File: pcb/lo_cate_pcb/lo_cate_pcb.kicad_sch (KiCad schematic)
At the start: 49 parts, among them J1 Conn_01x07_Pin, J2 690-005-299-043, J3 U.FL-R-SMT-110, SW1 MICRO_RESET, SW2 MICRO_ON, SW3 BUTTON1, SW4 BUTTON2, SW5 BUTTON3, U1 STM32F401RETx, U2 BMI323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

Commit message: Final PCB design done
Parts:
- removed J3: U.FL-R-SMT-110, footprints:CONN1_UFL-R_HIR, symbol 2024-06-24_09-28-13:U.FL-R-SMT-110
- added U8: 734120114, footprints:73412-0114_MOL, symbol 2024-06-27_09-08-45:734120114
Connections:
- net GND: now also U8.2 (GROUND), U8.3 (GROUND), U8.4 (GROUND)
- net at U6.9 (ANT): now also U8.1 (SIGNAL)

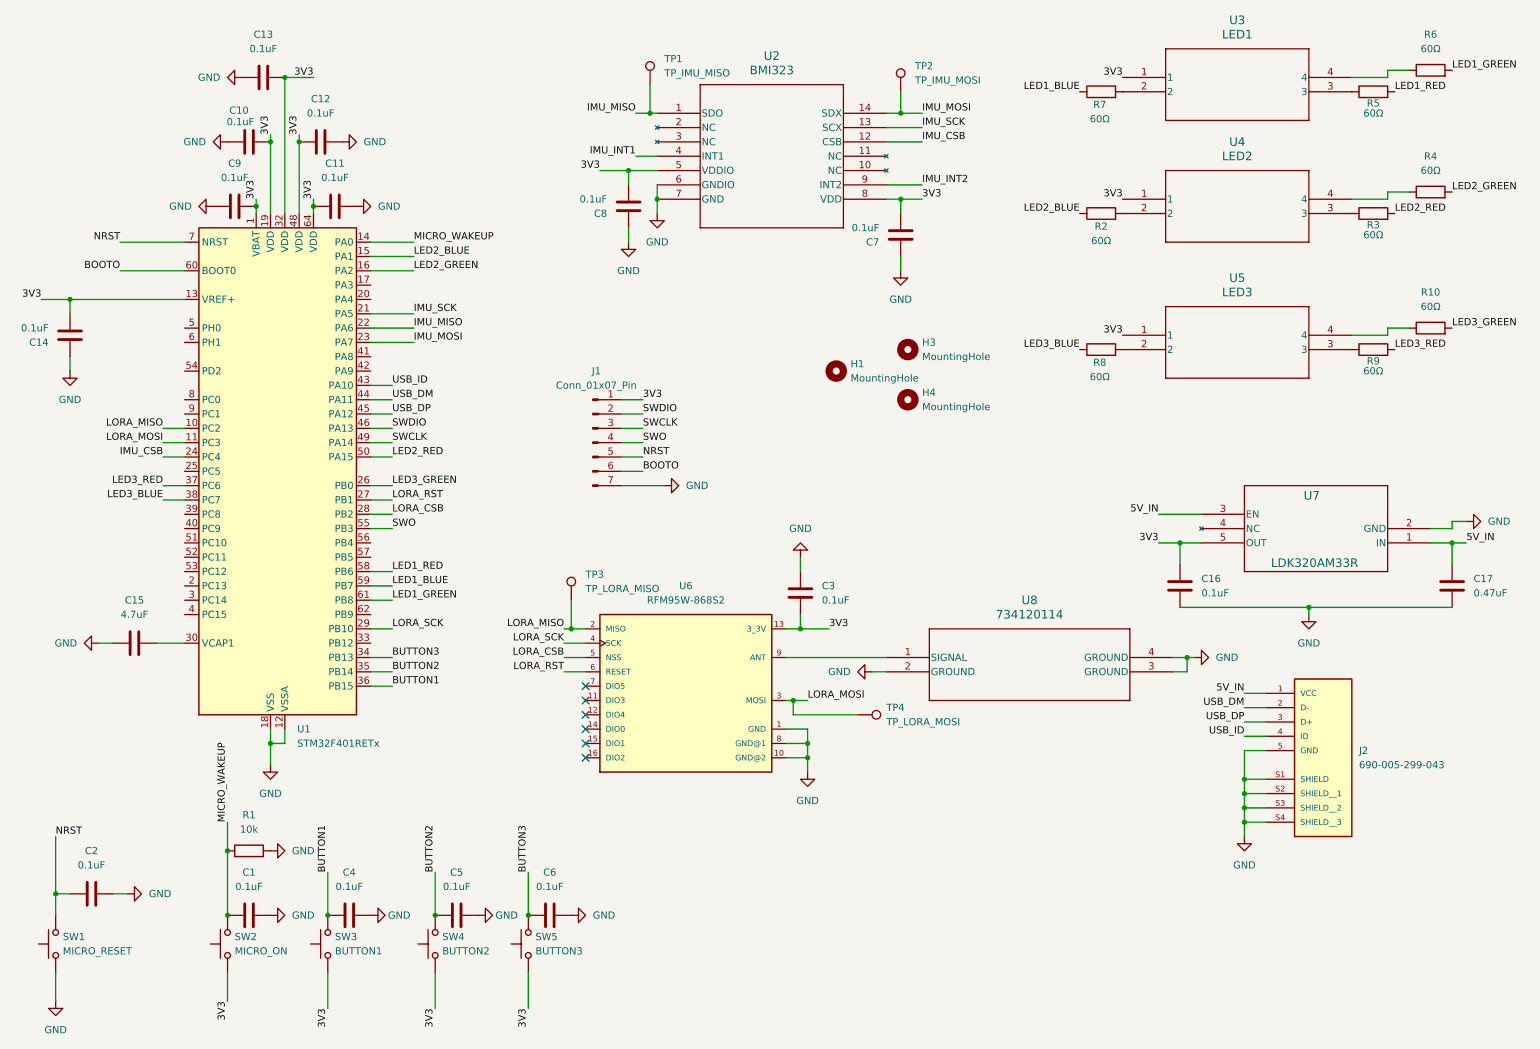
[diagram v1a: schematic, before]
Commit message: Changed PCB to a 4 Layer Version
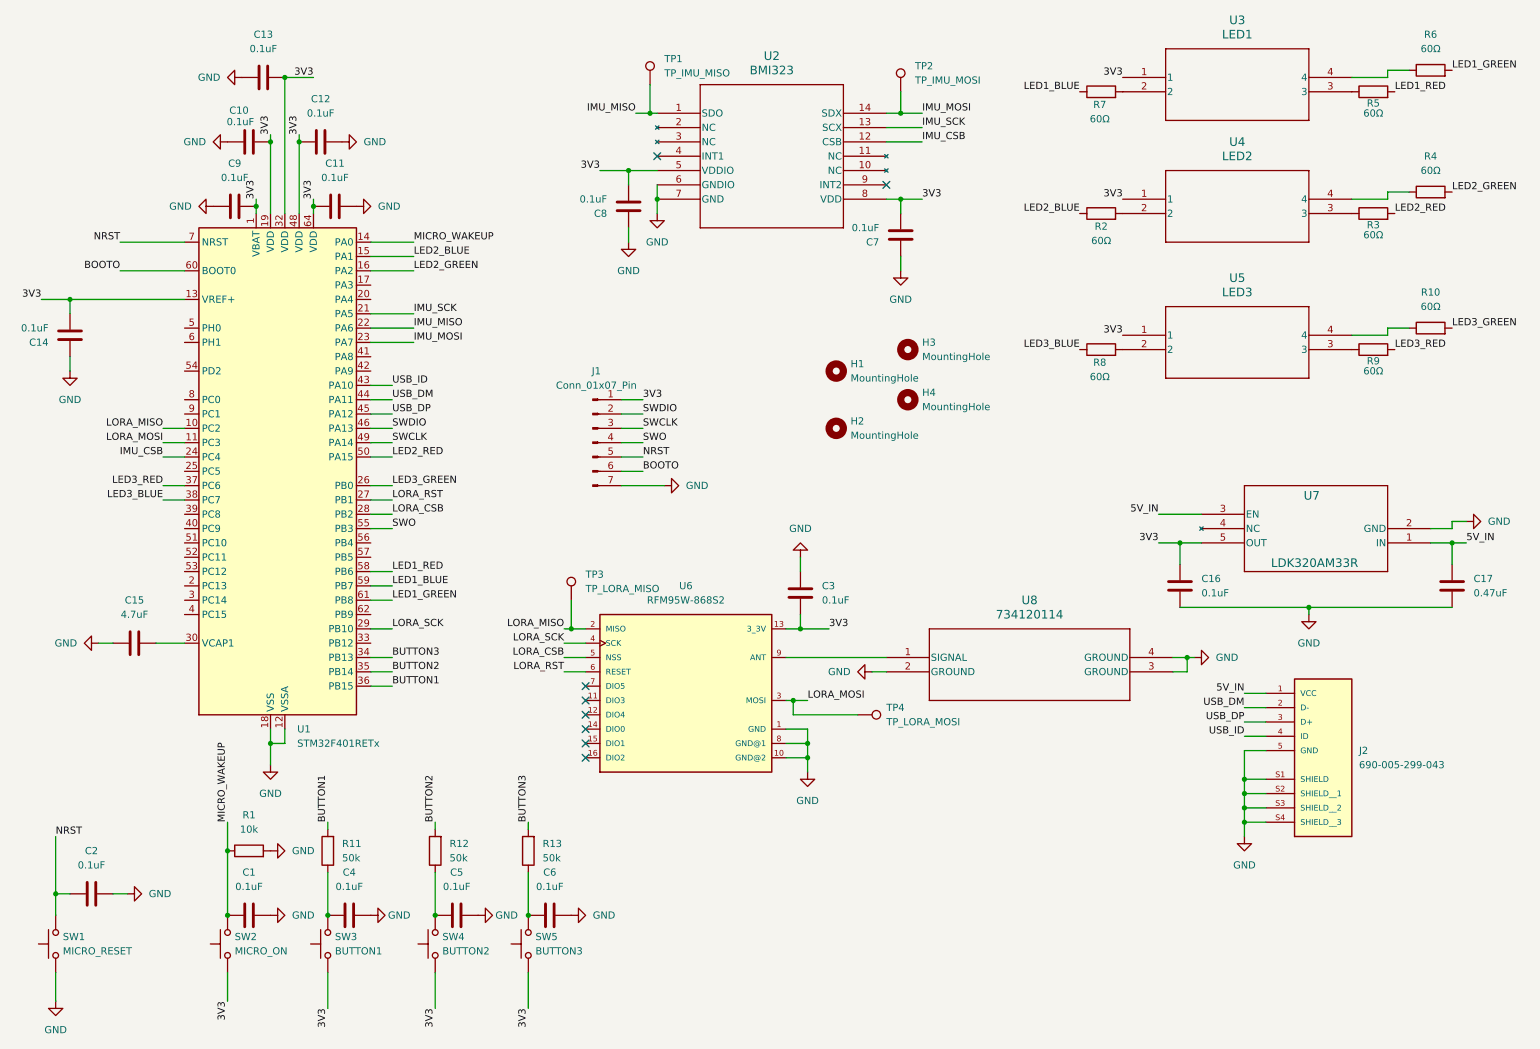
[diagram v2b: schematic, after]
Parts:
- added H2: MountingHole, MountingHole:MountingHole_3.2mm_M3, symbol Mechanical:MountingHole
- added R11, R12, R13: 50k, Resistor_SMD:R_0805_2012Metric_Pad1.20x1.40mm_HandSolder, symbol Device:R
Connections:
- net BUTTON1: now also R11.2; no longer C4.2, SW3.2
- net BUTTON2: now also R12.2; no longer C5.2, SW4.2
- net BUTTON3: now also R13.2; no longer C6.2, SW5.2
- net IMU_INT1: no longer names the net of U2.4 (INT1)
- net IMU_INT2: no longer names the net of U2.9 (INT2)
- new net: C4.2, R11.1, SW3.2
- new net: C6.2, R13.1, SW5.2
- new net: C5.2, R12.1, SW4.2
- no-connect marks 6 -> 8

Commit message: Added an external crystal oscillator
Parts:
- added C18, C19: 10p, Capacitor_SMD:C_0805_2012Metric_Pad1.18x1.45mm_HandSolder, symbol Device:C
- added R14: 30R, Resistor_SMD:R_0805_2012Metric_Pad1.20x1.40mm_HandSolder, symbol Device:R
- added Y1: Crystal_GND24_Small, Crystal:Crystal_SMD_7050-4Pin_7.0x5.0mm, symbol Device:Crystal_GND24_Small
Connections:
- net GND: now also C18.2, C19.2, Y1.2, Y1.4
- net OSC_IN: now reaches U1.5 (PH0)
- net OSC_IN: now also C18.1, Y1.1
- net OSC_OUT: now reaches U1.6 (PH1)
- net OSC_OUT: now also R14.2
- new net: C19.1, R14.1, Y1.3
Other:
- moved on the sheet: C16, C17, H1, H2, H3, H4, J1, J2, U7

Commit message: broke a usart to header pins
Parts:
- removed J1: Conn_01x07_Pin, Connector_PinHeader_1.27mm:PinHeader_1x07_P1.27mm_Vertical, symbol Connector:Conn_01x07_Pin
- added J3: Conn_01x09_Pin, Connector_PinSocket_1.27mm:PinSocket_1x09_P1.27mm_Vertical, symbol Connector:Conn_01x09_Pin
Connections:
- net 3V3: now also J3.1 (Pin_1)
- net BOOTO: now also J3.6 (Pin_6)
- net GND: now also J3.9 (Pin_9)
- net LED3_BLUE: now also U1.57 (PB5); no longer U1.38 (PC7)
- net LED3_RED: now also U1.56 (PB4); no longer U1.37 (PC6)
- net NRST: now also J3.5 (Pin_5)
- net SWCLK: now also J3.3 (Pin_3)
- net SWDIO: now also J3.2 (Pin_2)
- net SWO: now also J3.4 (Pin_4)
- new net UART_RX: J3.7 (Pin_7), U1.38 (PC7)
- new net UART_TX: J3.8 (Pin_8), U1.37 (PC6)
